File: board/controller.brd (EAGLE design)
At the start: 100 x 100 mm, 70 parts, among them J1 X, J10 FEED_HOLD, J11 PROBE, J12 ERROR, J13 HOLDING, J14 GND, J15 MOTOR_CURRENT, J16 SD_READER, J17 WHEEL, J19 Z_DISPLAY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

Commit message: release v1.0
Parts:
- moved C3 1.41 mm to (44.0, 13.8)
- moved J14 0.30 mm to (43.2, 4.06)
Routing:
- net VIN: track 58.3 -> 57.7 mm

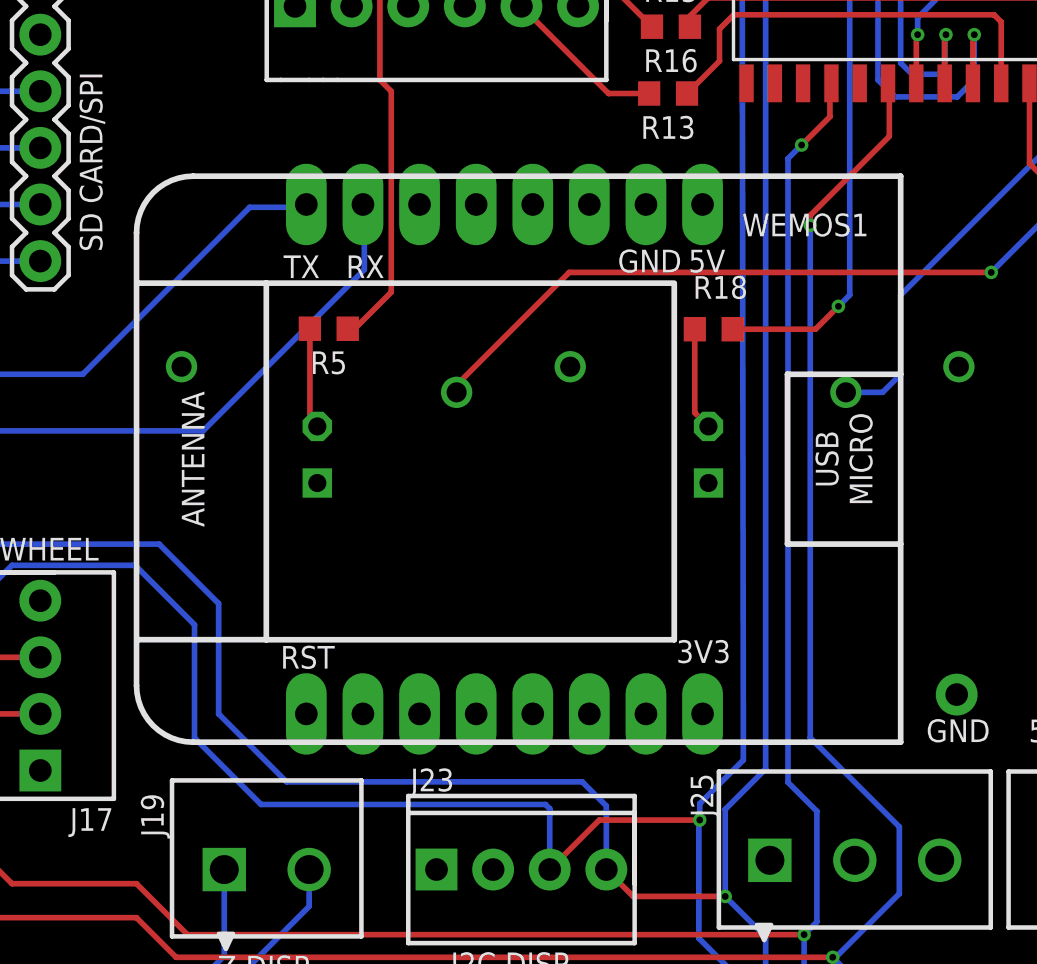
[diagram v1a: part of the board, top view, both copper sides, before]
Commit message: updated wemos silk, added info to notes
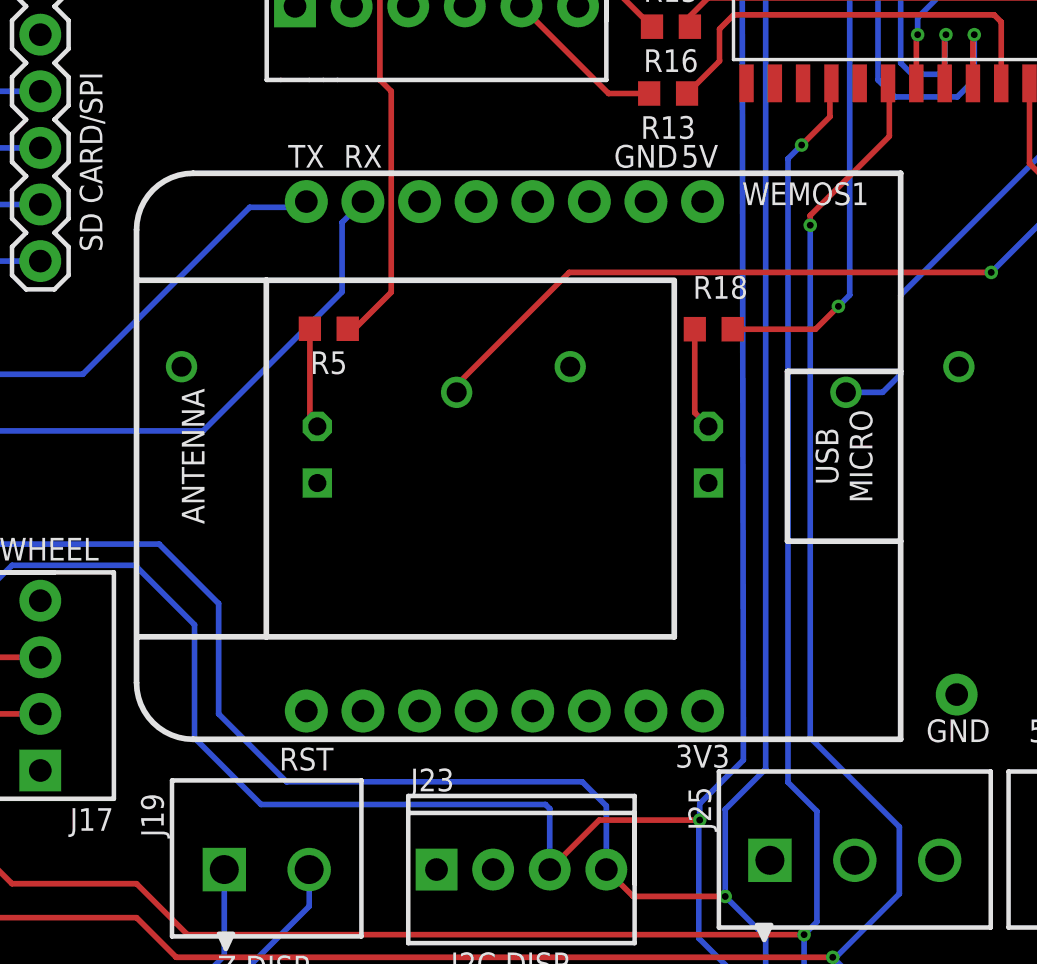
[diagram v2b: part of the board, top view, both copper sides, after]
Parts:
- moved WEMOS1 1.40 mm to (64.0, 63.6)
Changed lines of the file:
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@@
 <layer number="21" name="tPlace" color="7" fill="1" visible="yes" active="yes"/>
 <layer number="22" name="bPlace" color="7" fill="1" visible="yes" active="yes"/>
-<layer number="23" name="tOrigins" color="15" fill="1" visible="no" active="yes"/>
+<layer number="23" name="tOrigins" color="15" fill="1" visible="yes" active="yes"/>
 <layer number="24" name="bOrigins" color="15" fill="1" visible="no" active="yes"/>
 <layer number="25" name="tNames" color="7" fill="1" visible="yes" active="yes"/>
@@
 <text x="49.511" y="3.156" size="1.778" layer="21" ratio="21">+</text>
 <text x="37.085" y="3.185" size="1.778" layer="21" ratio="21" align="bottom-right">-</text>
-<dimension x1="100" y1="100" x2="0" y2="100" x3="50" y3="108" textsize="1.778" layer="51"/>
-<dimension x1="0" y1="100" x2="0" y2="0" x3="-8" y3="50" textsize="1.778" layer="51"/>
+<dimension x1="100" y1="100" x2="0" y2="100" x3="50" y3="104" textsize="1.778" layer="51"/>
+<dimension x1="0" y1="100" x2="0" y2="0" x3="-2" y3="50" textsize="1.778" layer="51"/>
 <text x="30.077" y="13.464" size="1.016" layer="21" ratio="21" align="center">Hyatt CNC Controller
 180804
@@
 <attribute name="NAME" x="96.505" y="13.53" size="1.016" layer="26" ratio="21" rot="MR0" align="center"/>
 </element>
-<element name="WEMOS1" library="holla" package="WEMOS-D1-MINI" value="" x="64.008" y="62.23" smashed="yes" rot="R90">
-<attribute name="NAME" x="75.94" y="74.518" size="1.016" layer="25" ratio="21" rot="R180" align="bottom-right"/>
+<element name="WEMOS1" library="holla" package="WEMOS-D1-MINI" value="" x="64.008" y="63.63" smashed="yes" rot="R90">
+<attribute name="NAME" x="75.94" y="75.918" size="1.016" layer="25" ratio="21" rot="R180" align="bottom-right"/>
 </element>
 <element name="J8" library="holla" package="CONN-.100-2" value="RESET" x="13.562" y="37.5505" smashed="yes" rot="R180">
@@
 </element>
 <element name="J25" library="holla" package="CONN-3.81MM-KF2EDG-3" value="GND" x="81" y="45.5" smashed="yes">
-<attribute name="NAME" x="74.651" y="47.4415" size="1.016" layer="25" font="vector" ratio="21" rot="R90"/>
+<attribute name="NAME" x="74.551" y="46.8415" size="1.016" layer="25" font="vector" ratio="21" rot="R90"/>
 <attribute name="VALUE" x="89.113" y="42.6415" size="1.016" layer="27" font="vector" ratio="21" rot="R90"/>
 </element>
@@
 <wire x1="38.1" y1="67.31" x2="46.355" y2="67.31" width="0.254" layer="16"/>
 <wire x1="46.355" y1="67.31" x2="53.848" y2="74.803" width="0.254" layer="16"/>
-<wire x1="53.848" y1="74.803" x2="56.261" y2="74.803" width="0.254" layer="16"/>
-<wire x1="56.261" y1="74.803" x2="56.388" y2="74.93" width="0.254" layer="16"/>
+<wire x1="53.848" y1="74.803" x2="56.131" y2="74.803" width="0.254" layer="16"/>
+<wire x1="56.131" y1="74.803" x2="56.388" y2="75.06" width="0.254" layer="16"/>
 </signal>
 <signal name="RADIO_RX">
@@
 <contactref element="U2" pad="1.1"/>
 <wire x1="38.1" y1="64.77" x2="51.7525" y2="64.77" width="0.254" layer="16"/>
-<wire x1="51.7525" y1="64.77" x2="58.9915" y2="72.009" width="0.254" layer="16"/>
-<wire x1="58.9915" y1="72.009" x2="58.9915" y2="74.8665" width="0.254" layer="16"/>
-<wire x1="58.9915" y1="74.8665" x2="58.928" y2="74.93" width="0.254" layer="16"/>
+<wire x1="51.7525" y1="64.77" x2="57.9915" y2="71.009" width="0.254" layer="16"/>
+<wire x1="57.9915" y1="71.009" x2="57.9915" y2="74.1235" width="0.254" layer="16"/>
+<wire x1="57.9915" y1="74.1235" x2="58.928" y2="75.06" width="0.254" layer="16"/>
 </signal>
 <signal name="FEED_OVERRIDE_OFF">

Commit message: added component values to schematic cleaned up brd layout
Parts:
- J18: value (none) -> FEED
- R1: value (none) -> 5.23k
- R10, R11, R12, R13, R14, R15, R16, R17, R18, R19, R22, R23, R24, R25, R26, R3, R4, R5, R6, R9: value (none) -> 220
- R2: value (none) -> 47k

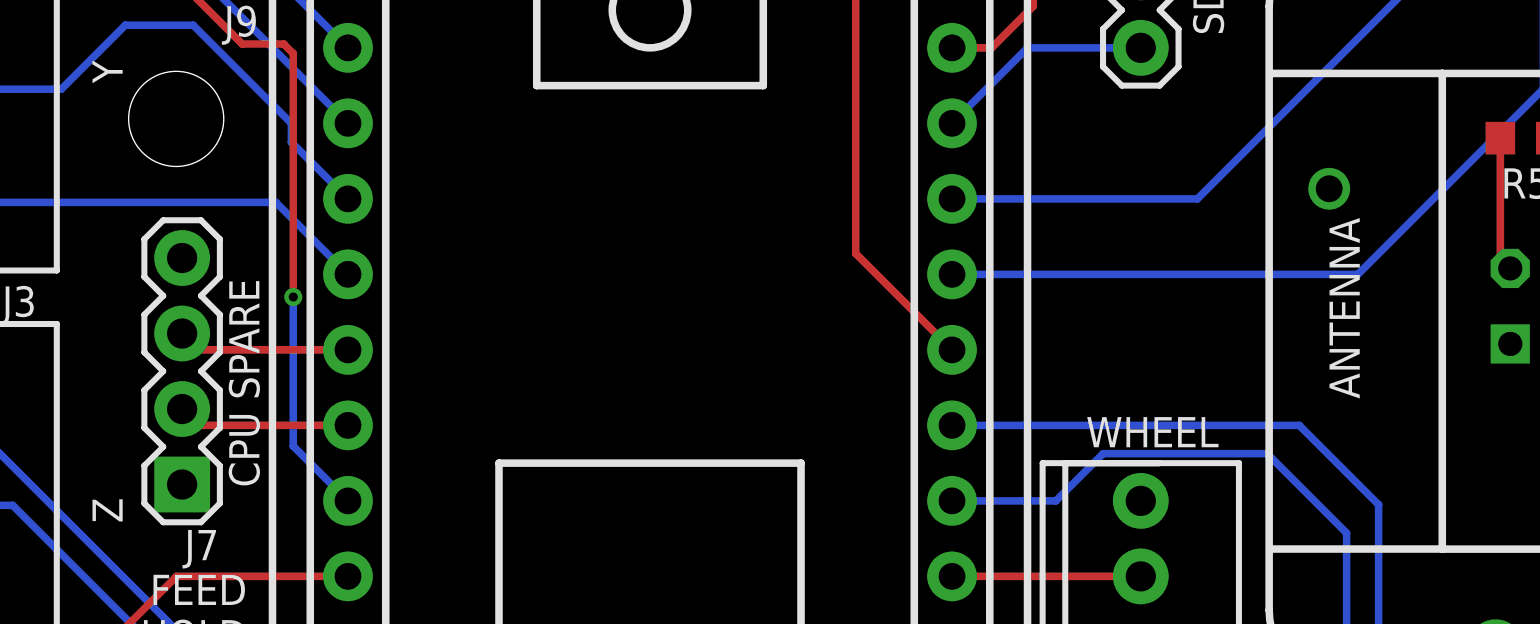
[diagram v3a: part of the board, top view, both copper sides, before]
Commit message: a little cleaning in main.c started v1.1 of schematic, v1.0 boards need blue-wired
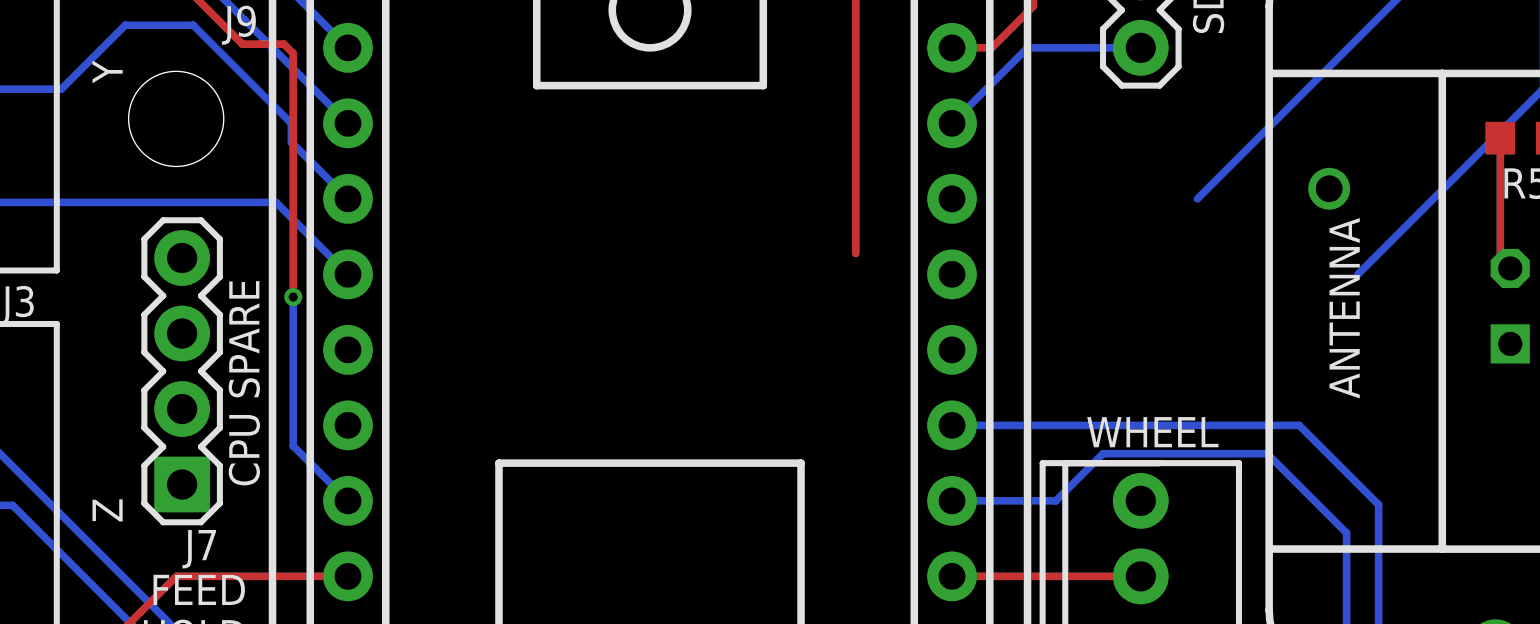
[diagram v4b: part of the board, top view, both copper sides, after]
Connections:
- removed net CPU_SPARE_IO_0: J7.3, U2.15.0
- removed net CPU_SPARE_IO_1: J7.2, U2.15.1
- net FEED_HOLDING_OUT: now also U2.1.2; no longer U2.1.0
- net RADIO_RX: now also J7.2, U2.15.1; no longer U2.1.1
- net RADIO_TX: now also J7.3, U2.15.0; no longer U2.1.2
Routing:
- net RADIO_RX: track 26.9 -> 13.3 mm
- net RADIO_TX: track 21.5 -> 13.2 mm
- net CPU_SPARE_IO_1: track 5.81 -> 0.00 mm
- net CPU_SPARE_IO_0: track 5.81 -> 0.00 mm
- net FEED_HOLDING_OUT: track 35.9 -> 31.3 mm
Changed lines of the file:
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@@
 <signal name="FEED_HOLDING_OUT">
 <contactref element="J13" pad="2"/>
-<contactref element="U2" pad="1.0"/>
 <wire x1="31.76" y1="95.5" x2="31.76" y2="85.207" width="0.254" layer="16"/>
 <wire x1="31.76" y1="85.207" x2="34.8615" y2="82.1055" width="0.254" layer="16"/>
 <via x="34.8615" y="82.1055" extent="1-16" drill="0.3048"/>
 <wire x1="34.8615" y1="82.1055" x2="34.8615" y2="65.4685" width="0.254" layer="1"/>
-<wire x1="34.8615" y1="65.4685" x2="38.1" y2="62.23" width="0.254" layer="1"/>
+<contactref element="U2" pad="1.2"/>
+<wire x1="34.8615" y1="65.4685" x2="38.1" y2="67.31" width="0" layer="19" extent="1-1"/>
 </signal>
 <signal name="Z_DISPLAY_RX_IN">
@@
 <signal name="RADIO_TX">
 <contactref element="WEMOS1" pad="TX"/>
-<contactref element="U2" pad="1.2"/>
-<wire x1="38.1" y1="67.31" x2="46.355" y2="67.31" width="0.254" layer="16"/>
 <wire x1="46.355" y1="67.31" x2="53.848" y2="74.803" width="0.254" layer="16"/>
 <wire x1="53.848" y1="74.803" x2="56.131" y2="74.803" width="0.254" layer="16"/>
 <wire x1="56.131" y1="74.803" x2="56.388" y2="75.06" width="0.254" layer="16"/>
+<contactref element="U2" pad="15.0"/>
+<contactref element="J7" pad="3"/>
+<wire x1="17.78" y1="62.23" x2="46.355" y2="67.31" width="0" layer="19" extent="16-16"/>
+<wire x1="12.2" y1="62.78" x2="17.78" y2="62.23" width="0" layer="19" extent="1-1"/>
 </signal>
 <signal name="RADIO_RX">
 <contactref element="WEMOS1" pad="RX"/>
-<contactref element="U2" pad="1.1"/>
-<wire x1="38.1" y1="64.77" x2="51.7525" y2="64.77" width="0.254" layer="16"/>
 <wire x1="51.7525" y1="64.77" x2="57.9915" y2="71.009" width="0.254" layer="16"/>
 <wire x1="57.9915" y1="71.009" x2="57.9915" y2="74.1235" width="0.254" layer="16"/>
 <wire x1="57.9915" y1="74.1235" x2="58.928" y2="75.06" width="0.254" layer="16"/>
+<contactref element="U2" pad="15.1"/>
+<contactref element="J7" pad="2"/>
+<wire x1="17.78" y1="59.69" x2="51.7525" y2="64.77" width="0" layer="19" extent="16-16"/>
+<wire x1="12.2" y1="60.24" x2="17.78" y2="59.69" width="0" layer="19" extent="1-1"/>
 </signal>
 <signal name="FEED_OVERRIDE_OFF">
@@
 <wire x1="44.45" y1="77.47" x2="38.1" y2="77.47" width="0.254" layer="16"/>
 </signal>
-<signal name="CPU_SPARE_IO_0">
-<contactref element="J7" pad="3"/>
-<contactref element="U2" pad="15.0"/>
-<wire x1="17.78" y1="62.23" x2="12.75" y2="62.23" width="0.254" layer="1"/>
-<wire x1="12.75" y1="62.23" x2="12.2" y2="62.78" width="0.254" layer="1"/>
-</signal>
-<signal name="CPU_SPARE_IO_1">
-<contactref element="J7" pad="2"/>
-<contactref element="U2" pad="15.1"/>
-<wire x1="17.78" y1="59.69" x2="12.75" y2="59.69" width="0.254" layer="1"/>
-<wire x1="12.75" y1="59.69" x2="12.2" y2="60.24" width="0.254" layer="1"/>
-</signal>
 <signal name="MIST_ENABLE_OUT">

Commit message: updated several net names in schematic and psoc changed I2C to fixed instead of UDB
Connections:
- net RADIO_TX renamed RADIO_TX_OUT
- net SPINDLE_SPEED renamed SPINDLE_SPEED_OUT
- new net RADIO_RX_IN: U2.15.1
- net RADIO_RX: no longer U2.15.1
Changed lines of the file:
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@@
 <wire x1="32.512" y1="34.798" x2="38.1" y2="29.21" width="0.254" layer="16"/>
 </signal>
-<signal name="RADIO_TX">
+<signal name="RADIO_TX_OUT">
 <contactref element="WEMOS1" pad="TX"/>
 <wire x1="46.355" y1="67.31" x2="53.848" y2="74.803" width="0.254" layer="16"/>
@@
 <wire x1="57.9915" y1="71.009" x2="57.9915" y2="74.1235" width="0.254" layer="16"/>
 <wire x1="57.9915" y1="74.1235" x2="58.928" y2="75.06" width="0.254" layer="16"/>
-<contactref element="U2" pad="15.1"/>
 <contactref element="J7" pad="2"/>
-<wire x1="17.78" y1="59.69" x2="51.7525" y2="64.77" width="0" layer="19" extent="16-16"/>
-<wire x1="12.2" y1="60.24" x2="17.78" y2="59.69" width="0" layer="19" extent="1-1"/>
+<wire x1="12.2" y1="60.24" x2="51.7525" y2="64.77" width="0" layer="19" extent="16-16"/>
 </signal>
 <signal name="FEED_OVERRIDE_OFF">
@@
 <wire x1="44.45" y1="24.13" x2="38.1" y2="24.13" width="0.254" layer="16"/>
 </signal>
-<signal name="SPINDLE_SPEED">
+<signal name="SPINDLE_SPEED_OUT">
 <contactref element="J6" pad="3"/>
 <contactref element="U2" pad="2.7"/>
@@
 <wire x1="14.95" y1="34" x2="17.78" y2="36.83" width="0.254" layer="1"/>
 </signal>
+<signal name="RADIO_RX_IN">
+<contactref element="U2" pad="15.1"/>
+</signal>
 </signals>

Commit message: updated a net name
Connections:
- removed net RADIO_RX: J7.2, WEMOS1.RX
- net RADIO_RX_IN: now also J7.2, WEMOS1.RX
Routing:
- net RADIO_RX_IN: track 0.00 -> 13.3 mm
- net RADIO_RX: track 13.3 -> 0.00 mm
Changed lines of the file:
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@@
 <wire x1="12.2" y1="62.78" x2="17.78" y2="62.23" width="0" layer="19" extent="1-1"/>
-</signal>
-<signal name="RADIO_RX">
-<contactref element="WEMOS1" pad="RX"/>
-<wire x1="51.7525" y1="64.77" x2="57.9915" y2="71.009" width="0.254" layer="16"/>
-<wire x1="57.9915" y1="71.009" x2="57.9915" y2="74.1235" width="0.254" layer="16"/>
-<wire x1="57.9915" y1="74.1235" x2="58.928" y2="75.06" width="0.254" layer="16"/>
-<contactref element="J7" pad="2"/>
-<wire x1="12.2" y1="60.24" x2="51.7525" y2="64.77" width="0" layer="19" extent="16-16"/>
 </signal>
 <signal name="FEED_OVERRIDE_OFF">
@@
 <signal name="RADIO_RX_IN">
 <contactref element="U2" pad="15.1"/>
+<contactref element="WEMOS1" pad="RX"/>
+<wire x1="51.7525" y1="64.77" x2="57.9915" y2="71.009" width="0.254" layer="16"/>
+<wire x1="57.9915" y1="71.009" x2="57.9915" y2="74.1235" width="0.254" layer="16"/>
+<wire x1="57.9915" y1="74.1235" x2="58.928" y2="75.06" width="0.254" layer="16"/>
+<contactref element="J7" pad="2"/>
+<wire x1="17.78" y1="59.69" x2="51.7525" y2="64.77" width="0" layer="19" extent="16-16"/>
+<wire x1="12.2" y1="60.24" x2="17.78" y2="59.69" width="0" layer="19" extent="1-1"/>
 </signal>
 </signals>

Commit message: don't know what changes are
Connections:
- new net MISC_ENABLE_OUT: J5.3
- net STEPPER_ENABLE_OUT: no longer J5.3
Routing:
- net STEPPER_ENABLE_OUT: track 19.1 -> 7.76 mm
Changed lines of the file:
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@@
 </signal>
 <signal name="STEPPER_ENABLE_OUT">
-<contactref element="J5" pad="3"/>
 <contactref element="U2" pad="0.4"/>
 <via x="12" y="34" extent="1-16" drill="0.3048"/>
 <wire x1="12" y1="34" x2="12" y2="33.19" width="0.254" layer="16"/>
-<wire x1="12" y1="33.19" x2="4" y2="25.19" width="0.254" layer="16"/>
 <wire x1="12" y1="34" x2="14.95" y2="34" width="0.254" layer="1"/>
 <wire x1="14.95" y1="34" x2="17.78" y2="36.83" width="0.254" layer="1"/>
@@
 <wire x1="12.2" y1="60.24" x2="17.78" y2="59.69" width="0" layer="19" extent="1-1"/>
 </signal>
+<signal name="MISC_ENABLE_OUT">
+<contactref element="J5" pad="3"/>
+</signal>
 </signals>
